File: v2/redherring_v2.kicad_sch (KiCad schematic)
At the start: 188 parts, among them J4 Pimaroni Trackball, Q2 TIP120, SW1 SW_PUSH_LED, SW10 SW_PUSH_LED, SW11 SW_PUSH_LED, SW12 SW_PUSH_LED, SW13 SW_PUSH_LED, SW14 SW_PUSH_LED, SW15 SW_PUSH_LED, SW16 SW_PUSH_LED, SW17 SW_PUSH_LED, SW18 SW_PUSH_LED, SW19 SW_PUSH_LED, SW2 SW_PUSH_LED, SW20 SW_PUSH_LED, SW21 SW_PUSH_LED, SW22 SW_PUSH_LED, SW23 SW_PUSH_LED, SW24 SW_PUSH_LED, SW25 SW_PUSH_LED, SW26 SW_PUSH_LED, SW27 SW_PUSH_LED, SW28 SW_PUSH_LED, SW29 SW_PUSH_LED, SW3 SW_PUSH_LED, SW30 SW_PUSH_LED, SW31 SW_PUSH_LED, SW32 SW_PUSH_LED, SW33 SW_PUSH_LED, SW34 SW_PUSH_LED, SW35 SW_PUSH_LED, SW36 SW_PUSH_LED, SW37 SW_PUSH_LED, SW38 SW_PUSH_LED, SW39 SW_PUSH_LED, SW4 SW_PUSH_LED, SW40 SW_PUSH_LED, SW41 SW_PUSH_LED, SW42 SW_PUSH_LED, SW43 SW_PUSH_LED, SW44 SW_PUSH_LED, SW45 SW_PUSH_LED, SW46 SW_PUSH_LED, SW47 SW_PUSH_LED, SW48 SW_PUSH_LED, SW49 SW_PUSH_LED, SW5 SW_PUSH_LED, SW50 SW_PUSH_LED, SW51 SW_PUSH_LED, SW52 SW_PUSH_LED, SW53 SW_PUSH_LED, SW54 SW_PUSH_LED, SW55 SW_PUSH_LED, SW56 SW_PUSH_LED, SW57 SW_PUSH_LED, SW58 SW_PUSH_LED, SW59 SW_PUSH_LED, SW6 SW_PUSH_LED, SW60 SW_PUSH_LED, SW61 SW_PUSH_LED, SW62 SW_PUSH_LED, SW63 SW_PUSH_LED, SW64 SW_PUSH_LED, SW65 SW_PUSH_LED, SW66 SW_PUSH_LED, SW67 SW_PUSH_LED, SW68 SW_PUSH_LED, SW69 SW_PUSH_LED, SW7 SW_PUSH_LED, SW70 SW_PUSH_LED, SW71 SW_PUSH_LED, SW72 SW_PUSH_LED, SW73 SW_PUSH_LED, SW74 SW_PUSH_LED, SW75 SW_PUSH_LED, SW76 SW_PUSH_LED, SW77 SW_PUSH_LED, SW78 SW_PUSH_LED, SW79 SW_PUSH_LED, SW8 SW_PUSH_LED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

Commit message: Fixed columns started LED wiring and routing
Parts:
- removed D70, D80, D90: D, red_herring_v2_footprints:D_SOD-123_DO-35_Hybrid_DoubleSided, symbol Device:D
- removed SW70, SW80, SW90: SW_PUSH_LED, red_herring_v2_footprints:V2_CherryMX_DS_Hotswap_miniE_1U_SEED_LH, symbol red_herring_v2:SW_PUSH_LED
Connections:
- net Col1 is gone; now on net col1: SW1.5, SW11.5, SW21.5, SW31.5, SW41.5, SW51.5, SW61.5, SW71.5, SW81.5
- net Col10 is gone; now on net col10: SW10.5, SW20.5, SW30.5, SW40.5, SW50.5, SW60.5
- net Col2 is gone; now on net col2: SW12.5, SW2.5, SW22.5, SW32.5, SW42.5, SW52.5, SW62.5, SW72.5, SW82.5
- net Col3 is gone; now on net col3: SW13.5, SW23.5, SW3.5, SW33.5, SW43.5, SW53.5, SW63.5, SW73.5, SW83.5
- net Col4 is gone; now on net col4: SW14.5, SW24.5, SW34.5, SW4.5, SW44.5, SW54.5, SW64.5, SW74.5, SW84.5
- net Col5 is gone; now on net col5: SW15.5, SW25.5, SW35.5, SW45.5, SW5.5, SW55.5, SW65.5, SW75.5, SW85.5
- net Col6 is gone; now on net col6: SW16.5, SW26.5, SW36.5, SW46.5, SW56.5, SW6.5, SW66.5, SW76.5, SW86.5
- net Col8 is gone; now on net col8: SW18.5, SW28.5, SW38.5, SW48.5, SW58.5, SW68.5, SW78.5, SW8.5, SW88.5
- net col9 is gone; now on net row7: U3.29 (GPIO22)
- net GND: now also SW27.5, SW37.5, SW47.5, SW57.5, SW67.5, SW77.5, SW87.5
- net LED: now also SW7.4 (DIN), U3.34 (GPIO28_ADC2); no longer U3.24 (GPIO18)
- net VDD: now also SW40.4 (DIN)
- net col1: now also U3.1 (GPIO0); no longer U3.12 (GPIO9)
- net col2: now also U3.2 (GPIO1); no longer U3.14 (GPIO10)
- net col3: now also U3.4 (GPIO2); no longer U3.15 (GPIO11)
- net col4: now also U3.5 (GPIO3); no longer U3.16 (GPIO12)
- net col5: now also U3.6 (GPIO4); no longer U3.17 (GPIO13)
- net col6: now also U3.7 (GPIO5); no longer U3.19 (GPIO14)
- net col7: now also SW17.4 (DIN), SW7.5, U3.9 (GPIO6); no longer U3.20 (GPIO15)
- net col8: now also U3.12 (GPIO9); no longer U3.34 (GPIO28_ADC2)
- net row1: now also U3.20 (GPIO15); no longer U3.1 (GPIO0)
- net row2: now also U3.19 (GPIO14); no longer U3.2 (GPIO1)
- net row3: now also U3.17 (GPIO13); no longer U3.4 (GPIO2)
- net row4: now also U3.16 (GPIO12); no longer U3.5 (GPIO3)
- net row5: now also U3.15 (GPIO11); no longer U3.6 (GPIO4)
- net row6: now also U3.14 (GPIO10); no longer U3.7 (GPIO5)
- net row7: no longer U3.9 (GPIO6)
- net row8: now also U3.24 (GPIO18); no longer U3.10 (GPIO7)
- net row9: now also U3.10 (GPIO7); no longer U3.11 (GPIO8)
- net at SW75.2 (DOUT): now also SW79.4 (DIN)
- net at SW75.4 (DIN): now also SW74.2 (DOUT)
- net at SW20.2 (DOUT): now also SW19.4 (DIN)
- net at SW20.4 (DIN): now also SW65.2 (DOUT)
- net at SW30.2 (DOUT): now also SW71.4 (DIN)
- net at SW30.4 (DIN): now also SW29.2 (DOUT)
- net at SW71.2 (DOUT): now also SW72.4 (DIN)
- net at SW76.4 (DIN): now also SW77.2 (DOUT)
- net at SW19.2 (DOUT): now also SW18.4 (DIN)
- net at SW62.2 (DOUT): now also SW63.4 (DIN)
- net at SW62.4 (DIN): now also SW61.2 (DOUT)
- net at SW74.4 (DIN): now also SW73.2 (DOUT)
- net at SW65.4 (DIN): now also SW66.2 (DOUT)
- net at SW77.4 (DIN): now also SW78.2 (DOUT)
- net at SW17.6: no longer D17.2 (A)
- net at SW73.4 (DIN): now also SW72.2 (DOUT)
- net at SW79.2 (DOUT): now also SW78.4 (DIN)
- net at SW9.2 (DOUT): now also SW10.4 (DIN)
- net at SW9.4 (DIN): now also SW8.2 (DOUT)
- net at SW63.2 (DOUT): now also SW64.4 (DIN)
- net at SW10.2 (DOUT): now also SW61.4 (DIN)
- net at SW7.2 (DOUT): now also SW8.4 (DIN)
- net at SW28.2 (DOUT): now also SW29.4 (DIN)
- net at SW28.4 (DIN): now also SW27.2 (DOUT)
- net at SW68.2 (DOUT): now also SW67.4 (DIN)
- net at SW68.4 (DIN): now also SW69.2 (DOUT)
- net at SW66.4 (DIN): now also SW67.2 (DOUT)
- net at SW69.4 (DIN): now also SW64.2 (DOUT)
- removed net Col7: SW17.5, SW27.5, SW37.5, SW47.5, SW57.5, SW67.5, SW7.5, SW77.5, SW87.5
- net Col9 renamed SW89A
- net SW89A: now also U3.11 (GPIO8)
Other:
- moved on the sheet: SW17A, SW17B, SW8B

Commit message: LED wiring first pass complete
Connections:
- net 5V is gone; now on net VCC: D_SOL_1.C, J_SOL_1.2 (Pin_2), U3.40 (VBUS)
- net GND: no longer SW27.5, SW37.5, SW47.5, SW57.5, SW67.5, SW77.5, SW87.5
- net VCC: no longer U3.39 (VSYS)
- net VDD: no longer SW40.4 (DIN)
- net col7: now also SW17.6, SW27.5, SW37.5, SW47.5, SW57.5, SW67.5, SW77.5, SW87.5; no longer SW17.4 (DIN)
- net at SW60.2 (DOUT): now also SW81.4 (DIN)
- net at SW60.4 (DIN): now also SW59.2 (DOUT)
- net at SW45.2 (DOUT): now also SW46.4 (DIN)
- net at SW45.4 (DIN): now also SW44.2 (DOUT)
- net at SW11.2 (DOUT): now also SW51.4 (DIN)
- net at SW11.4 (DIN): now also SW12.2 (DOUT)
- net at SW85.2 (DOUT): now also SW84.4 (DIN)
- net at SW85.4 (DIN): now also SW86.2 (DOUT)
- net at SW24.2 (DOUT): now also SW25.4 (DIN)
- net at SW24.4 (DIN): now also SW23.2 (DOUT)
- net at SW87.2 (DOUT): now also SW86.4 (DIN)
- net at SW87.4 (DIN): now also SW88.2 (DOUT)
- net at SW59.4 (DIN): now also SW50.2 (DOUT)
- net at SW53.2 (DOUT): now also SW52.4 (DIN)
- net at SW53.4 (DIN): now also SW54.2 (DOUT)
- net at SW81.2 (DOUT): now also SW82.4 (DIN)
- net at SW38.2 (DOUT): now also SW37.4 (DIN)
- net at SW38.4 (DIN): now also SW39.2 (DOUT)
- net at SW17.2 (DOUT): now also SW27.4 (DIN)
- net at SW58.2 (DOUT): now also SW57.4 (DIN)
- net at SW58.4 (DIN): now also SW84.2 (DOUT)
- net at SW43.2 (DOUT): now also SW44.4 (DIN)
- net at SW43.4 (DIN): now also SW42.2 (DOUT)
- net at SW82.2 (DOUT): now also SW83.4 (DIN)
- net at SW51.2 (DOUT): now also SW1.4 (DIN)
- net at SW26.2 (DOUT): now also SW16.4 (DIN)
- net at SW26.4 (DIN): now also SW25.2 (DOUT)
- net at SW55.2 (DOUT): now also SW54.4 (DIN)
- net at SW55.4 (DIN): now also SW56.2 (DOUT)
- net at SW33.2 (DOUT): now also SW32.4 (DIN)
- net at SW33.4 (DIN): now also SW34.2 (DOUT)
- net at SW52.2 (DOUT): now also SW41.4 (DIN)
- net at SW76.2 (DOUT): now also SW40.4 (DIN)
- net at SW32.2 (DOUT): now also SW31.4 (DIN)
- net at SW39.4 (DIN): now also SW40.2 (DOUT)
- net at SW50.4 (DIN): now also SW49.2 (DOUT)
- net at SW15.2 (DOUT): now also SW14.4 (DIN)
- net at SW15.4 (DIN): now also SW16.2 (DOUT)
- net at SW6.4 (DIN): now also SW5.2 (DOUT)
- net at SW12.4 (DIN): now also SW13.2 (DOUT)
- net at SW49.4 (DIN): now also SW48.2 (DOUT)
- net at SW21.2 (DOUT): now also SW22.4 (DIN)
- net at SW21.4 (DIN): now also SW31.2 (DOUT)
- net at SW22.2 (DOUT): now also SW23.4 (DIN)
- net at SW41.2 (DOUT): now also SW42.4 (DIN)
- net at SW13.4 (DIN): now also SW14.2 (DOUT)
- net at SW17.5: now also D17.2 (A)
- net at SW47.2 (DOUT): now also SW36.4 (DIN)
- net at SW47.4 (DIN): now also SW46.2 (DOUT)
- net at SW48.4 (DIN): now also SW37.2 (DOUT)
- net at SW35.2 (DOUT): now also SW34.4 (DIN)
- net at SW35.4 (DIN): now also SW36.2 (DOUT)
- net at SW3.2 (DOUT): now also SW4.4 (DIN)
- net at SW3.4 (DIN): now also SW2.2 (DOUT)
- net at SW4.2 (DOUT): now also SW5.4 (DIN)
- net at SW57.2 (DOUT): now also SW56.4 (DIN)
- net at SW88.4 (DIN): now also SW83.2 (DOUT)
- net at SW1.2 (DOUT): now also SW2.4 (DIN)
- net at SW18.2 (DOUT): now also SW17.4 (DIN)

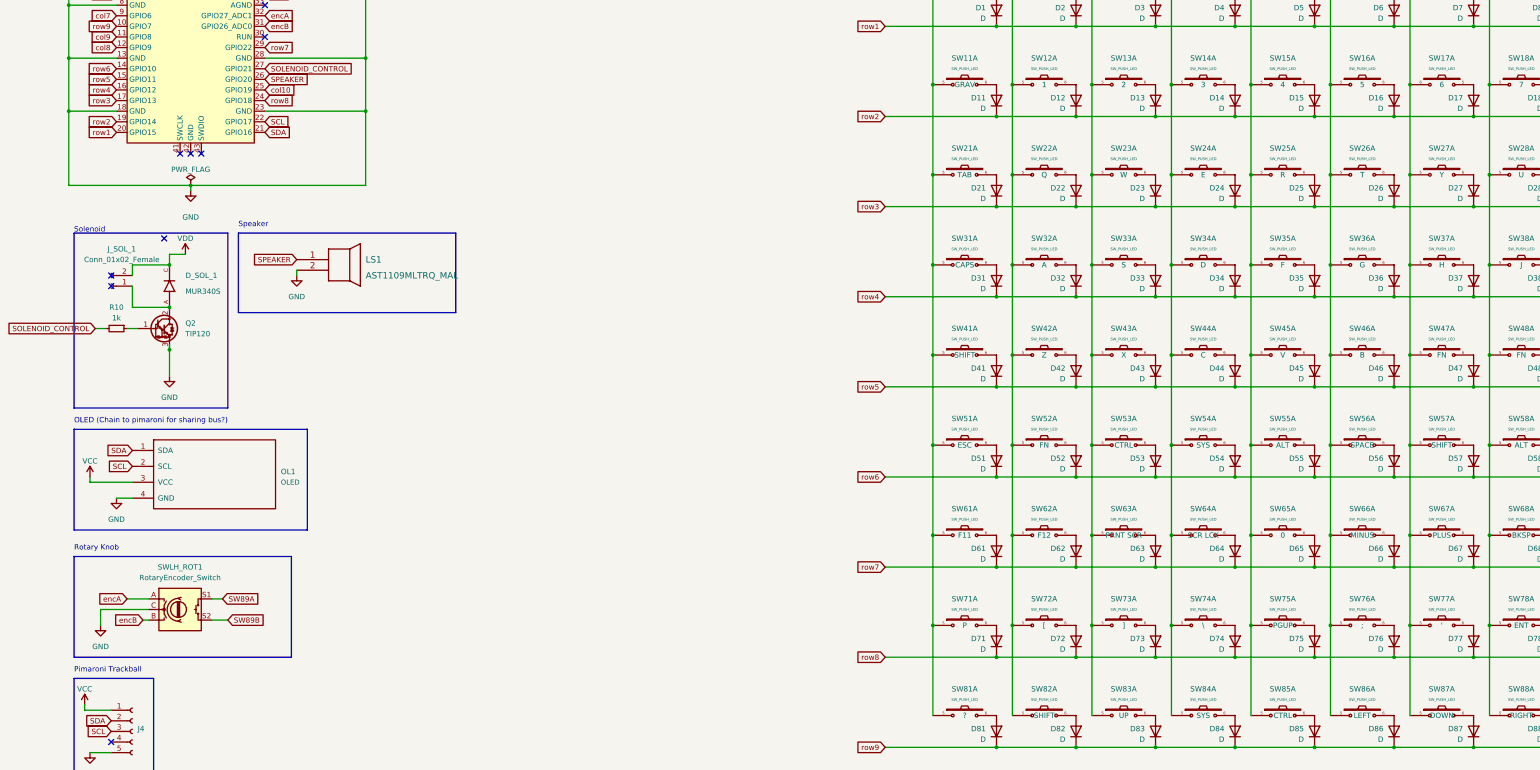
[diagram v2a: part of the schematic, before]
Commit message: First pass wiring complete reworked pimoroni fixed outline
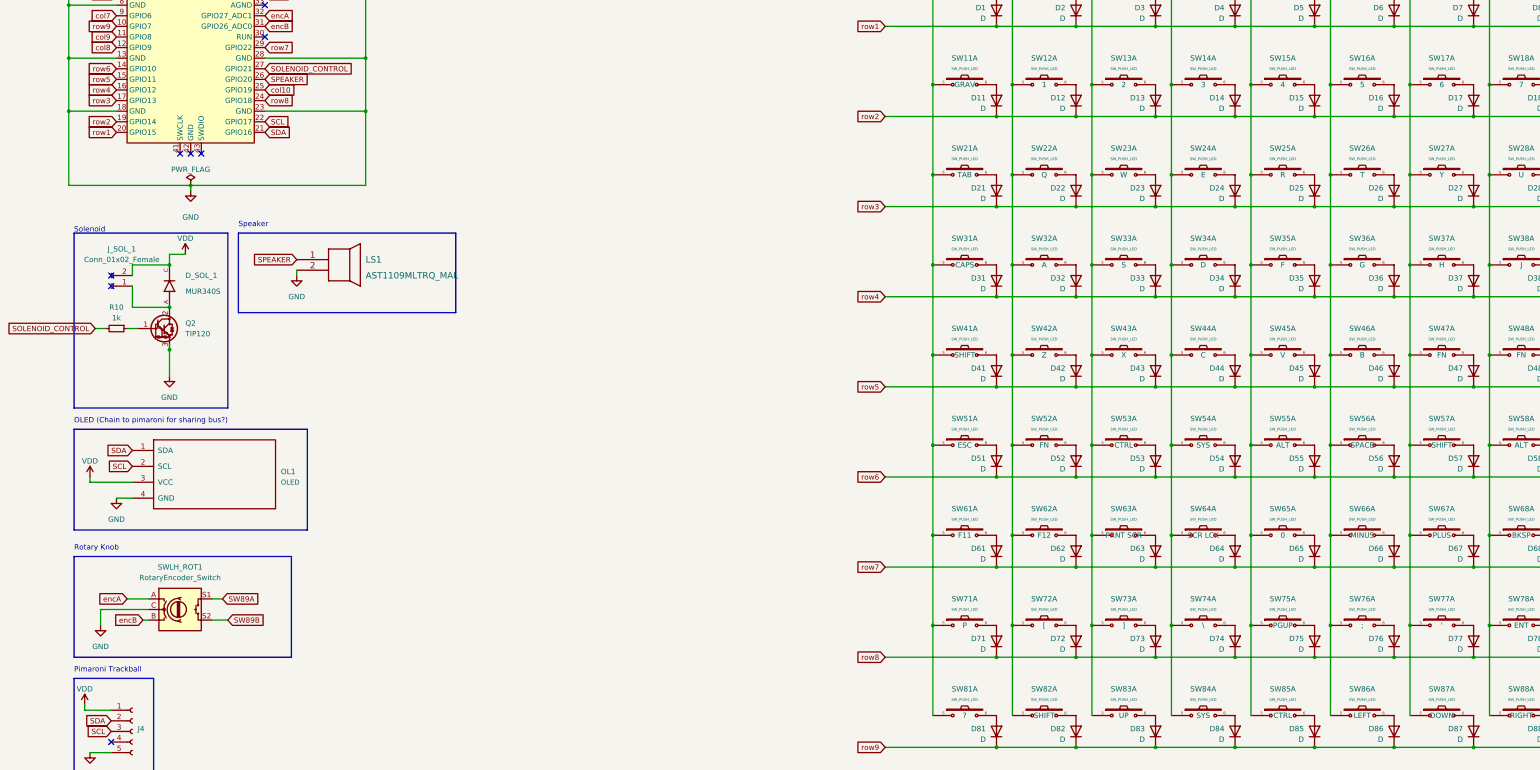
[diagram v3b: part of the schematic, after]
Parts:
- J4: footprint ergodonk_kicad_library:pimoroni_trackball -> red_herring_v2_footprints:pimoroni_trackball
- Q2: footprint Package_TO_SOT_THT:TO-220-3_Vertical -> red_herring_v2_footprints:Tip 120 with heatsink
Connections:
- net VCC is gone; now on net VDD: D_SOL_1.C, J4.1 (Pin_1), J_SOL_1.2 (Pin_2), OL1.3 (VCC), U3.40 (VBUS)
- net col7: now also SW17.5; no longer SW17.6
- net at D17.2 (A): now also SW17.6; no longer SW17.5
- no-connect marks 12 -> 11
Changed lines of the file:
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@@
   (junction (at 261.62 124.46) (diameter 0) (color 0 0 0 0)
   )
-  (junction (at 69.85 19.05) (diameter 0) (color 0 0 0 0)
-  )
   (junction (at 375.92 38.1) (diameter 0) (color 0 0 0 0)
   )
@@
   (junction (at 238.76 175.26) (diameter 0) (color 0 0 0 0)
   )
+  (junction (at 69.85 19.05) (diameter 0) (color 0 0 0 0)
+  )
   (junction (at 238.76 153.67) (diameter 0) (color 0 0 0 0)
   )
@@
   (no_connect (at 63.5 33.02))
   (no_connect (at 63.5 30.48))
-  (no_connect (at 39.37 96.52))
   (wire (pts (xy 238.76 196.85) (xy 257.81 196.85))
     (stroke (width 0) (type default))
@@
     )
   )
-  (symbol (lib_id "power:VCC") (at 20.32 208.28 0) (unit 1)
-    (in_bom yes) (on_board yes) (dnp no)
-    (property "Reference" "#PWR030" (at 20.32 212.09 0)
-      (effects (font (size 1.27 1.27)) hide)
-    )
-    (property "Value" "VCC" (at 20.32 204.47 0)
-      (effects (font (size 1.27 1.27)))
-    )
-    (property "Footprint" "" (at 20.32 208.28 0)
-      (effects (font (size 1.27 1.27)) hide)
-    )
-    (property "Datasheet" "" (at 20.32 208.28 0)
-      (effects (font (size 1.27 1.27)) hide)
-    )
-    (pin "1")
-    (instances
-      (project "redherring_v2"
-        (path "/ac76b486-7d71-4fdd-84d6-1ecd5326b6c6"
-          (reference "#PWR030") (unit 1)
-        )
-      )
-      (project "ergodonk_pcb"
-        (path "/ed1aaf15-4e1f-4159-b371-d99b3fb972ad"
-          (reference "#PWR011") (unit 1)
-        )
-      )
-    )
-  )
   (symbol (lib_id "kbd:OLED") (at 50.8 153.67 0) (unit 1)
     (in_bom yes) (on_board yes) (dnp no) (fields_autoplaced)
@@
     )
   )
-  (symbol (lib_id "power:VCC") (at 69.85 19.05 0) (unit 1)
-    (in_bom yes) (on_board yes) (dnp no)
-    (property "Reference" "#PWR026" (at 69.85 22.86 0)
-      (effects (font (size 1.27 1.27)) hide)
-    )
-    (property "Value" "VDD" (at 69.85 15.24 0)
-      (effects (font (size 1.27 1.27)))
-    )
-    (property "Footprint" "" (at 69.85 19.05 0)
-      (effects (font (size 1.27 1.27)) hide)
-    )
-    (property "Datasheet" "" (at 69.85 19.05 0)
-      (effects (font (size 1.27 1.27)) hide)
-    )
-    (pin "1")
-    (instances
-      (project "redherring_v2"
-        (path "/ac76b486-7d71-4fdd-84d6-1ecd5326b6c6"
-          (reference "#PWR026") (unit 1)
-        )
-      )
-      (project "ergodonk_pcb"
-        (path "/ed1aaf15-4e1f-4159-b371-d99b3fb972ad"
-          (reference "#PWR021") (unit 1)
-        )
-      )
-    )
-  )
   (symbol (lib_id "red_herring_v2:SW_PUSH_LED") (at 364.49 102.87 0) (unit 1)
     (in_bom yes) (on_board yes) (dnp no) (fields_autoplaced)
@@
     )
   )
+  (symbol (lib_id "power:VDD") (at 69.85 19.05 0) (unit 1)
+    (in_bom yes) (on_board yes) (dnp no) (fields_autoplaced)
+    (property "Reference" "#PWR04" (at 69.85 22.86 0)
+      (effects (font (size 1.27 1.27)) hide)
+    )
+    (property "Value" "VDD" (at 69.85 15.24 0)
+      (effects (font (size 1.27 1.27)))
+    )
+    (property "Footprint" "" (at 69.85 19.05 0)
+      (effects (font (size 1.27 1.27)) hide)
+    )
+    (property "Datasheet" "" (at 69.85 19.05 0)
+      (effects (font (size 1.27 1.27)) hide)
+    )
+    (pin "1")
+    (instances
+      (project "redherring_v2"
+        (path "/ac76b486-7d71-4fdd-84d6-1ecd5326b6c6"
+          (reference "#PWR04") (unit 1)
+        )
+      )
+    )
+  )
   (symbol (lib_id "red_herring_v2:SW_PUSH_LED") (at 231.14 124.46 0) (unit 1)
     (in_bom yes) (on_board yes) (dnp no) (fields_autoplaced)
@@
       (effects (font (size 1.27 1.27)) (justify left))
     )
-    (property "Footprint" "Package_TO_SOT_THT:TO-220-3_Vertical" (at 43.18 120.015 0)
+    (property "Footprint" "red_herring_v2_footprints:Tip 120 with heatsink" (at 43.18 120.015 0)
       (effects (font (size 1.27 1.27) italic) (justify left) hide)
     )
@@
     )
   )
-  (symbol (lib_id "red_herring_v2:SW_PUSH_LED") (at 345.44 59.69 0) (mirror y) (unit 1)
+  (symbol (lib_id "red_herring_v2:SW_PUSH_LED") (at 345.44 59.69 0) (unit 1)
     (in_bom yes) (on_board yes) (dnp no)
     (property "Reference" "SW17" (at 345.44 53.34 0)
@@
       (effects (font (size 0.635 0.635)))
     )
-    (property "Footprint" "red_herring_v2_footprints:V2_CherryMX_DS_Hotswap_miniE_1U_SEED_LH" (at 344.678 54.61 0)
+    (property "Footprint" "red_herring_v2_footprints:V2_CherryMX_DS_Hotswap_miniE_1U_SEED_LH" (at 346.202 54.61 0)
       (effects (font (size 1.27 1.27)) hide)
     )
@@
     )
   )
+  (symbol (lib_id "power:VDD") (at 44.45 100.33 0) (unit 1)
+    (in_bom yes) (on_board yes) (dnp no) (fields_autoplaced)
+    (property "Reference" "#PWR01" (at 44.45 104.14 0)
+      (effects (font (size 1.27 1.27)) hide)
+    )
+    (property "Value" "VDD" (at 44.45 96.52 0)
+      (effects (font (size 1.27 1.27)))
+    )
+    (property "Footprint" "" (at 44.45 100.33 0)
+      (effects (font (size 1.27 1.27)) hide)
+    )
+    (property "Datasheet" "" (at 44.45 100.33 0)
+      (effects (font (size 1.27 1.27)) hide)
+    )
+    (pin "1")
+    (instances
+      (project "redherring_v2"
+        (path "/ac76b486-7d71-4fdd-84d6-1ecd5326b6c6"
+          (reference "#PWR01") (unit 1)
+        )
+      )
+    )
+  )
   (symbol (lib_id "red_herring_v2:SW_PUSH_LED") (at 601.98 128.27 0) (mirror y) (unit 2)
     (in_bom yes) (on_board yes) (dnp no)
@@
     )
   )
-  (symbol (lib_id "power:VCC") (at 21.59 153.67 0) (unit 1)
-    (in_bom yes) (on_board yes) (dnp no)
-    (property "Reference" "#PWR032" (at 21.59 157.48 0)
-      (effects (font (size 1.27 1.27)) hide)
-    )
-    (property "Value" "VCC" (at 21.59 149.86 0)
-      (effects (font (size 1.27 1.27)))
-    )
-    (property "Footprint" "" (at 21.59 153.67 0)
-      (effects (font (size 1.27 1.27)) hide)
-    )
-    (property "Datasheet" "" (at 21.59 153.67 0)
-      (effects (font (size 1.27 1.27)) hide)
-    )
-    (pin "1")
-    (instances
-      (project "redherring_v2"
-        (path "/ac76b486-7d71-4fdd-84d6-1ecd5326b6c6"
-          (reference "#PWR032") (unit 1)
-        )
-      )
-      (project "ergodonk_pcb"
-        (path "/ed1aaf15-4e1f-4159-b371-d99b3fb972ad"
-          (reference "#PWR017") (unit 1)
-        )
-      )
-    )
-  )
   (symbol (lib_id "red_herring_v2:SW_PUSH_LED") (at 231.14 59.69 0) (unit 1)
     (in_bom yes) (on_board yes) (dnp no) (fields_autoplaced)
@@
     )
   )
+  (symbol (lib_id "power:VDD") (at 21.59 153.67 0) (unit 1)
+    (in_bom yes) (on_board yes) (dnp no) (fields_autoplaced)
+    (property "Reference" "#PWR03" (at 21.59 157.48 0)
+      (effects (font (size 1.27 1.27)) hide)
+    )
+    (property "Value" "VDD" (at 21.59 149.86 0)
+      (effects (font (size 1.27 1.27)))
+    )
+    (property "Footprint" "" (at 21.59 153.67 0)
+      (effects (font (size 1.27 1.27)) hide)
+    )
+    (property "Datasheet" "" (at 21.59 153.67 0)
+      (effects (font (size 1.27 1.27)) hide)
+    )
+    (pin "1")
+    (instances
+      (project "redherring_v2"
+        (path "/ac76b486-7d71-4fdd-84d6-1ecd5326b6c6"
+          (reference "#PWR03") (unit 1)
+        )
+      )
+    )
+  )
   (symbol (lib_id "red_herring_v2:SW_PUSH_LED") (at 525.78 106.68 0) (unit 2)
     (in_bom yes) (on_board yes) (dnp no) (fields_autoplaced)
@@
     )
   )
+  (symbol (lib_id "power:VDD") (at 20.32 208.28 0) (unit 1)
+    (in_bom yes) (on_board yes) (dnp no) (fields_autoplaced)
+    (property "Reference" "#PWR02" (at 20.32 212.09 0)
+      (effects (font (size 1.27 1.27)) hide)
+    )
+    (property "Value" "VDD" (at 20.32 204.47 0)
+      (effects (font (size 1.27 1.27)))
+    )
+    (property "Footprint" "" (at 20.32 208.28 0)
+      (effects (font (size 1.27 1.27)) hide)
+    )
+    (property "Datasheet" "" (at 20.32 208.28 0)
+      (effects (font (size 1.27 1.27)) hide)
+    )
+    (pin "1")
+    (instances
+      (project "redherring_v2"
+        (path "/ac76b486-7d71-4fdd-84d6-1ecd5326b6c6"
+          (reference "#PWR02") (unit 1)
+        )
+      )
+    )
+  )
   (symbol (lib_id "red_herring_v2:SW_PUSH_LED") (at 506.73 63.5 0) (unit 2)
     (in_bom yes) (on_board yes) (dnp no) (fields_autoplaced)
@@
     )
   )
-  (symbol (lib_id "power:VCC") (at 44.45 100.33 0) (unit 1)
-    (in_bom yes) (on_board yes) (dnp no)
-    (property "Reference" "#PWR01" (at 44.45 104.14 0)
-      (effects (font (size 1.27 1.27)) hide)
-    )
-    (property "Value" "VDD" (at 44.45 96.52 0)
-      (effects (font (size 1.27 1.27)))
-    )
-    (property "Footprint" "" (at 44.45 100.33 0)
-      (effects (font (size 1.27 1.27)) hide)
-    )
-    (property "Datasheet" "" (at 44.45 100.33 0)
-      (effects (font (size 1.27 1.27)) hide)
-    )
-    (pin "1")
-    (instances
-      (project "redherring_v2"
-        (path "/ac76b486-7d71-4fdd-84d6-1ecd5326b6c6"
-          (reference "#PWR01") (unit 1)
-        )
-      )
-      (project "ergodonk_pcb"
-        (path "/ed1aaf15-4e1f-4159-b371-d99b3fb972ad"
-          (reference "#PWR021") (unit 1)
-        )
-      )
-    )
-  )
   (symbol (lib_id "Device:D") (at 314.96 193.04 270) (mirror x) (unit 1)
     (in_bom yes) (on_board yes) (dnp no)
@@
       (effects (font (size 1.27 1.27)) (justify left) hide)
     )
-    (property "Footprint" "ergodonk_kicad_library:pimoroni_trackball" (at 31.75 214.63 0)
+    (property "Footprint" "red_herring_v2_footprints:pimoroni_trackball" (at 31.75 214.63 0)
       (effects (font (size 1.27 1.27)) hide)
     )

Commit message: Updated diode footprint updated 3d models for diode and tip120
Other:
- note added: "The LEDs are wired according to board shape, so it gets a big ugly."
- note added: "The grid does not mirror the board shape. This was intentional, and allows for the maximum amount of grid intersections using the smallest amount of pins. There are 3 unused intersections."
- note added: "Unused matrix intersections. (You can add 3 keys here)"
- note removed: "Unused matrix intersections. (You can add keys here)"
- moved on the sheet: D1, D10, D11, D12, D13, D14, D15, D16, D17, D18, D19, D2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
